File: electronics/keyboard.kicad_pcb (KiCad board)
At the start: 2 copper layers, 171 parts, among them J1 CONN_02X10, SW1 SW_Push, SW10 SW_Push, SW11 SW_Push, SW12 SW_Push, SW13 SW_Push, SW14 SW_Push, SW15 SW_Push, SW16 SW_Push, SW17 SW_Push, SW18 SW_Push, SW19 SW_Push, SW20 SW_Push, SW21 SW_Push, SW22 SW_Push, SW23 SW_Push, SW24 SW_Push, SW25 SW_Push, SW27 SW_Push, SW28 SW_Push, SW29 SW_Push, SW3 SW_Push, SW30 SW_Push, SW31 SW_Push, SW32 SW_Push, SW33 SW_Push, SW34 SW_Push, SW35 SW_Push, SW36 SW_Push, SW37 SW_Push, SW38 SW_Push, SW39 SW_Push, SW4 SW_Push, SW40 SW_Push, SW41 SW_Push, SW42 SW_Push, SW43 SW_Push, SW44 SW_Push, SW45 SW_Push, SW46 SW_Push, SW47 SW_Push, SW48 SW_Push, SW49 SW_Push, SW5 SW_Push, SW50 SW_Push, SW51 SW_Push, SW52 SW_Push, SW53 SW_Push, SW54 SW_Push, SW55 SW_Push, SW56 SW_Push, SW57 SW_Push, SW58 SW_Push, SW59 SW_Push, SW6 SW_Push, SW60 SW_Push, SW61 SW_Push, SW62 SW_Push, SW63 SW_Push, SW64 SW_Push, SW65 SW_Push, SW66 SW_Push, SW67 SW_Push, SW68 SW_Push, SW69 SW_Push, SW7 SW_Push, SW70 SW_Push, SW71 SW_Push, SW72 SW_Push, SW73 SW_Push, SW74 SW_Push, SW75 SW_Push, SW76 SW_Push, SW77 SW_Push, SW78 SW_Push, SW8 SW_Push, SW81 SW_Push, SW82 SW_Push, SW83 SW_Push, SW84 SW_Push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

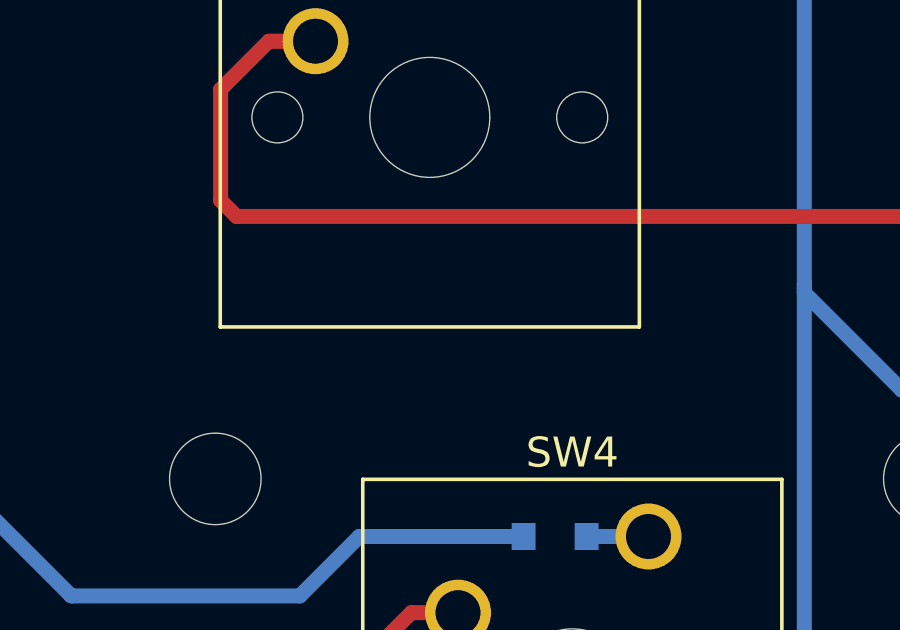
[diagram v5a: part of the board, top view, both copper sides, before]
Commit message: kicad5 fix and shift led in schematic
- Fixed schematic for kicad5
- added shift led in schematic
Todo
- Layout the led
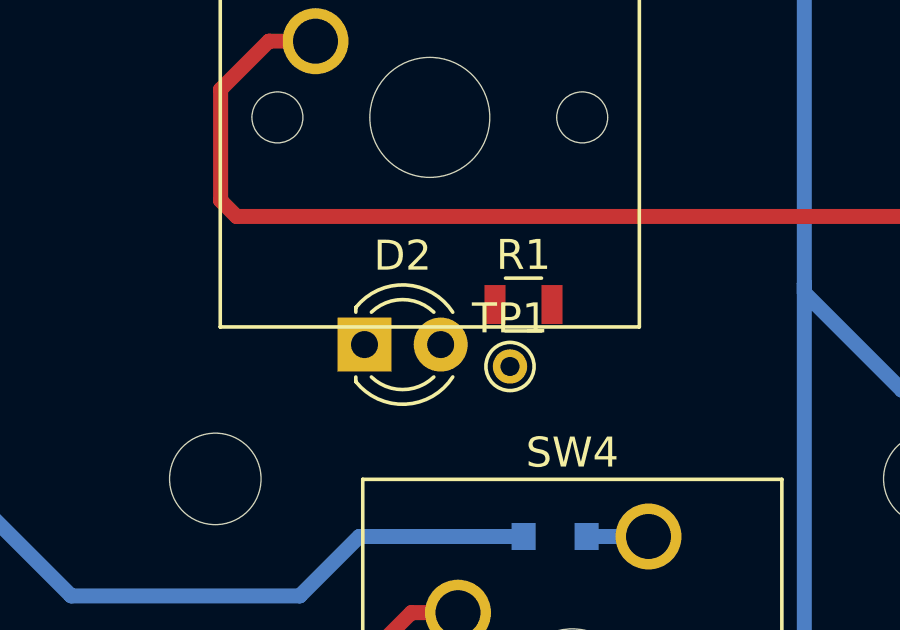
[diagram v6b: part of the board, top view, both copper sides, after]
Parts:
- added D2: LED, LEDs:LED_D3.0mm, F.Cu at (40.5, 184.1)
- added R1: 10k, Resistors_SMD:R_0805, F.Cu at (45.8, 182.8)
- added TP1: TestPoint, Connectors:PINTST, F.Cu at (45.3, 184.8)
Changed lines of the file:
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@@
     (tracks 1423)
     (zones 0)
-    (modules 171)
-    (nets 106)
+    (modules 174)
+    (nets 108)
   )
   (page A3)
@@
   (net 103 "Net-(D6-Pad2)")
   (net 104 /SwitchMatrix/COL11)
-  (net 105 "Net-(J1-Pad1)")
+  (net 105 "Net-(D2-Pad2)")
+  (net 106 "Net-(D2-Pad1)")
+  (net 107 "Net-(R1-Pad2)")
   (net_class Default "This is the default net class."
     (clearance 0.2)
@@
     (uvia_dia 0.3)
     (uvia_drill 0.1)
-    (add_net "Net-(J1-Pad1)")
+    (add_net "Net-(D2-Pad1)")
+    (add_net "Net-(D2-Pad2)")
+    (add_net "Net-(R1-Pad2)")
   )
   (net_class Double ""
@@
     (fp_line (start 3.9 6.6) (end -3.9 6.6) (layer B.CrtYd) (width 0.05))
     (pad 1 smd rect (at -2.585 5.715) (size 2.1 0.75) (layers B.Cu B.Mask)
-      (net 105 "Net-(J1-Pad1)"))
+      (net 105 "Net-(D2-Pad2)"))
     (pad 2 smd rect (at 2.585 5.715) (size 2.1 0.75) (layers B.Cu B.Mask)
       (net 92 /PB0))
@@
     (pad 1 np_thru_hole circle (at 0 0) (size 3.2 3.2) (drill 3.2) (layers *.Cu *.Mask))
   )
+  (module LEDs:LED_D3.0mm (layer F.Cu)
+    (at 40.483001 184.103001)
+    (descr "LED, diameter 3.0mm, 2 pins")
+    (tags "LED diameter 3.0mm 2 pins")
+    (fp_text reference D2 (at 1.27 -2.96) (layer F.SilkS)
+      (effects (font (size 1 1) (thickness 0.15)))
+    )
+    (fp_text value LED (at 1.27 2.96) (layer F.Fab)
+      (effects (font (size 1 1) (thickness 0.15)))
+    )
+    (fp_line (start 3.7 -2.25) (end -1.15 -2.25) (layer F.CrtYd) (width 0.05))
+    (fp_line (start 3.7 2.25) (end 3.7 -2.25) (layer F.CrtYd) (width 0.05))
+    (fp_line (start -1.15 2.25) (end 3.7 2.25) (layer F.CrtYd) (width 0.05))
+    (fp_line (start -1.15 -2.25) (end -1.15 2.25) (layer F.CrtYd) (width 0.05))
+    (fp_line (start -0.29 1.08) (end -0.29 1.236) (layer F.SilkS) (width 0.12))
+    (fp_line (start -0.29 -1.236) (end -0.29 -1.08) (layer F.SilkS) (width 0.12))
+    (fp_line (start -0.23 -1.16619) (end -0.23 1.16619) (layer F.Fab) (width 0.1))
+    (fp_circle (center 1.27 0) (end 2.77 0) (layer F.Fab) (width 0.1))
+    (fp_arc (start 1.27 0) (end 0.229039 1.08) (angle -87.9) (layer F.SilkS) (width 0.12))
+    (fp_arc (start 1.27 0) (end 0.229039 -1.08) (angle 87.9) (layer F.SilkS) (width 0.12))
+    (fp_arc (start 1.27 0) (end -0.29 1.235516) (angle -108.8) (layer F.SilkS) (width 0.12))
+    (fp_arc (start 1.27 0) (end -0.29 -1.235516) (angle 108.8) (layer F.SilkS) (width 0.12))
+    (fp_arc (start 1.27 0) (end -0.23 -1.16619) (angle 284.3) (layer F.Fab) (width 0.1))
+    (pad 2 thru_hole circle (at 2.54 0) (size 1.8 1.8) (drill 0.9) (layers *.Cu *.Mask)
+      (net 105 "Net-(D2-Pad2)"))
+    (pad 1 thru_hole rect (at 0 0) (size 1.8 1.8) (drill 0.9) (layers *.Cu *.Mask)
+      (net 106 "Net-(D2-Pad1)"))
+    (model ${KISYS3DMOD}/LEDs.3dshapes/LED_D3.0mm.wrl
+      (at (xyz 0 0 0))
+      (scale (xyz 0.393701 0.393701 0.393701))
+      (rotate (xyz 0 0 0))
+    )
+  )
+  (module Resistors_SMD:R_0805 (layer F.Cu)
+    (at 45.783001 182.768001)
+    (descr "Resistor SMD 0805, reflow soldering, Vishay (see dcrcw.pdf)")
+    (tags "resistor 0805")
+    (attr smd)
+    (fp_text reference R1 (at 0 -1.65) (layer F.SilkS)
+      (effects (font (size 1 1) (thickness 0.15)))
+    )
+    (fp_text value 10k (at 0 1.75) (layer F.Fab)
+      (effects (font (size 1 1) (thickness 0.15)))
+    )
+    (fp_line (start 1.55 0.9) (end -1.55 0.9) (layer F.CrtYd) (width 0.05))
+    (fp_line (start 1.55 0.9) (end 1.55 -0.9) (layer F.CrtYd) (width 0.05))
+    (fp_line (start -1.55 -0.9) (end -1.55 0.9) (layer F.CrtYd) (width 0.05))
+    (fp_line (start -1.55 -0.9) (end 1.55 -0.9) (layer F.CrtYd) (width 0.05))
+    (fp_line (start -0.6 -0.88) (end 0.6 -0.88) (layer F.SilkS) (width 0.12))
+    (fp_line (start 0.6 0.88) (end -0.6 0.88) (layer F.SilkS) (width 0.12))
+    (fp_line (start -1 -0.62) (end 1 -0.62) (layer F.Fab) (width 0.1))
+    (fp_line (start 1 -0.62) (end 1 0.62) (layer F.Fab) (width 0.1))
+    (fp_line (start 1 0.62) (end -1 0.62) (layer F.Fab) (width 0.1))
+    (fp_line (start -1 0.62) (end -1 -0.62) (layer F.Fab) (width 0.1))
+    (fp_text user %R (at 0 0) (layer F.Fab)
+      (effects (font (size 0.5 0.5) (thickness 0.075)))
+    )
+    (pad 2 smd rect (at 0.95 0) (size 0.7 1.3) (layers F.Cu F.Paste F.Mask)
+      (net 107 "Net-(R1-Pad2)"))
+    (pad 1 smd rect (at -0.95 0) (size 0.7 1.3) (layers F.Cu F.Paste F.Mask)
+      (net 106 "Net-(D2-Pad1)"))
+    (model ${KISYS3DMOD}/Resistors_SMD.3dshapes/R_0805.wrl
+      (at (xyz 0 0 0))
+      (scale (xyz 1 1 1))
+      (rotate (xyz 0 0 0))
+    )
+  )
+  (module Connectors:PINTST (layer F.Cu)
+    (at 45.333001 184.833001)
+    (descr "module 1 pin (ou trou mecanique de percage)")
+    (tags DEV)
+    (fp_text reference TP1 (at 0 -1.6) (layer F.SilkS)
+      (effects (font (size 1 1) (thickness 0.15)))
+    )
+    (fp_text value TestPoint (at 0 1.6) (layer F.Fab)
+      (effects (font (size 1 1) (thickness 0.15)))
+    )
+    (fp_circle (center 0 0) (end -0.254 -0.762) (layer F.SilkS) (width 0.12))
+    (fp_circle (center 0 0) (end 0.4 0.6) (layer F.Fab) (width 0.1))
+    (fp_circle (center 0 0) (end 1.1 0) (layer F.CrtYd) (width 0.05))
+    (pad 1 thru_hole circle (at 0 0) (size 1.143 1.143) (drill 0.635) (layers *.Cu *.Mask)
+      (net 107 "Net-(R1-Pad2)"))
+    (model ${KISYS3DMOD}/Connectors.3dshapes/PINTST.wrl
+      (at (xyz 0 0 0))
+      (scale (xyz 1 1 1))
+      (rotate (xyz 0 0 0))
+    )
+  )
   (gr_text "Change min Via " (at 59.908 237.028) (layer Dwgs.User)

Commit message: Updated PCB
Initial finished version
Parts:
- added REF**: MountingHole_3.2mm_M3, Mounting_Holes:MountingHole_3.2mm_M3, F.Cu at (310.9, 100.0)
- added REF**: MountingHole_3.2mm_M3, Mounting_Holes:MountingHole_3.2mm_M3, F.Cu at (45.9, 100.0)
- moved TP1 15.1 mm to (30.3, 183.6), turned to 90 degrees
- moved R1 12.1 mm to (33.7, 182.0), turned to 180 degrees
- moved REF** 10.0 mm to (310.9, 229.0)
- moved REF** 9.89 mm to (45.9, 229.0)
- moved D2 2.31 mm to (41.5, 182.0)
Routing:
- net Net-(D2-Pad2): track 0.00 -> 269.4 mm, vias 0 -> 2
- net Net-(D2-Pad1): track 0.00 -> 6.85 mm
- net Net-(R1-Pad2): track 0.00 -> 3.11 mm
- net /PB7: track 430.2 -> 430.7 mm
- net /PC0: track 492.3 -> 492.8 mm
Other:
- board text removed: "Change min Via"

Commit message: Added PCB outline in edge cut layer
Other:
- board outline added: 305 x 144.2 mm
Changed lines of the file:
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@@
   (general
     (thickness 1.6)
-    (drawings 1859)
+    (drawings 1866)
     (tracks 1447)
     (zones 0)
@@
     )
   )
+  (gr_line (start 315.708 89.828) (end 330.808 104.928) (layer Edge.Cuts) (width 0.15))
+  (gr_line (start 41.108 89.828) (end 315.708 89.828) (layer Edge.Cuts) (width 0.15))
+  (gr_line (start 26.108 104.828) (end 41.108 89.828) (layer Edge.Cuts) (width 0.15))
+  (gr_line (start 25.908 105.028) (end 26.108 104.828) (layer Edge.Cuts) (width 0.15))
+  (gr_line (start 25.908 234.028) (end 25.908 105.028) (layer Edge.Cuts) (width 0.15))
+  (gr_line (start 330.908 234.028) (end 25.908 234.028) (layer Edge.Cuts) (width 0.15))
+  (gr_line (start 330.808 104.928) (end 330.908 234.028) (layer Edge.Cuts) (width 0.15))
   (dimension 144 (width 0.3) (layer Dwgs.User)
     (gr_text "144.000 mm" (at 353.258 162.028 90) (layer Dwgs.User)
